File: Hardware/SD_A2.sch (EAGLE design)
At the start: 23 parts, among them IC1 74LS245N, IC2 LM1117DTX-3.3, IC3 28C64ASO, IC4 XC9572XL

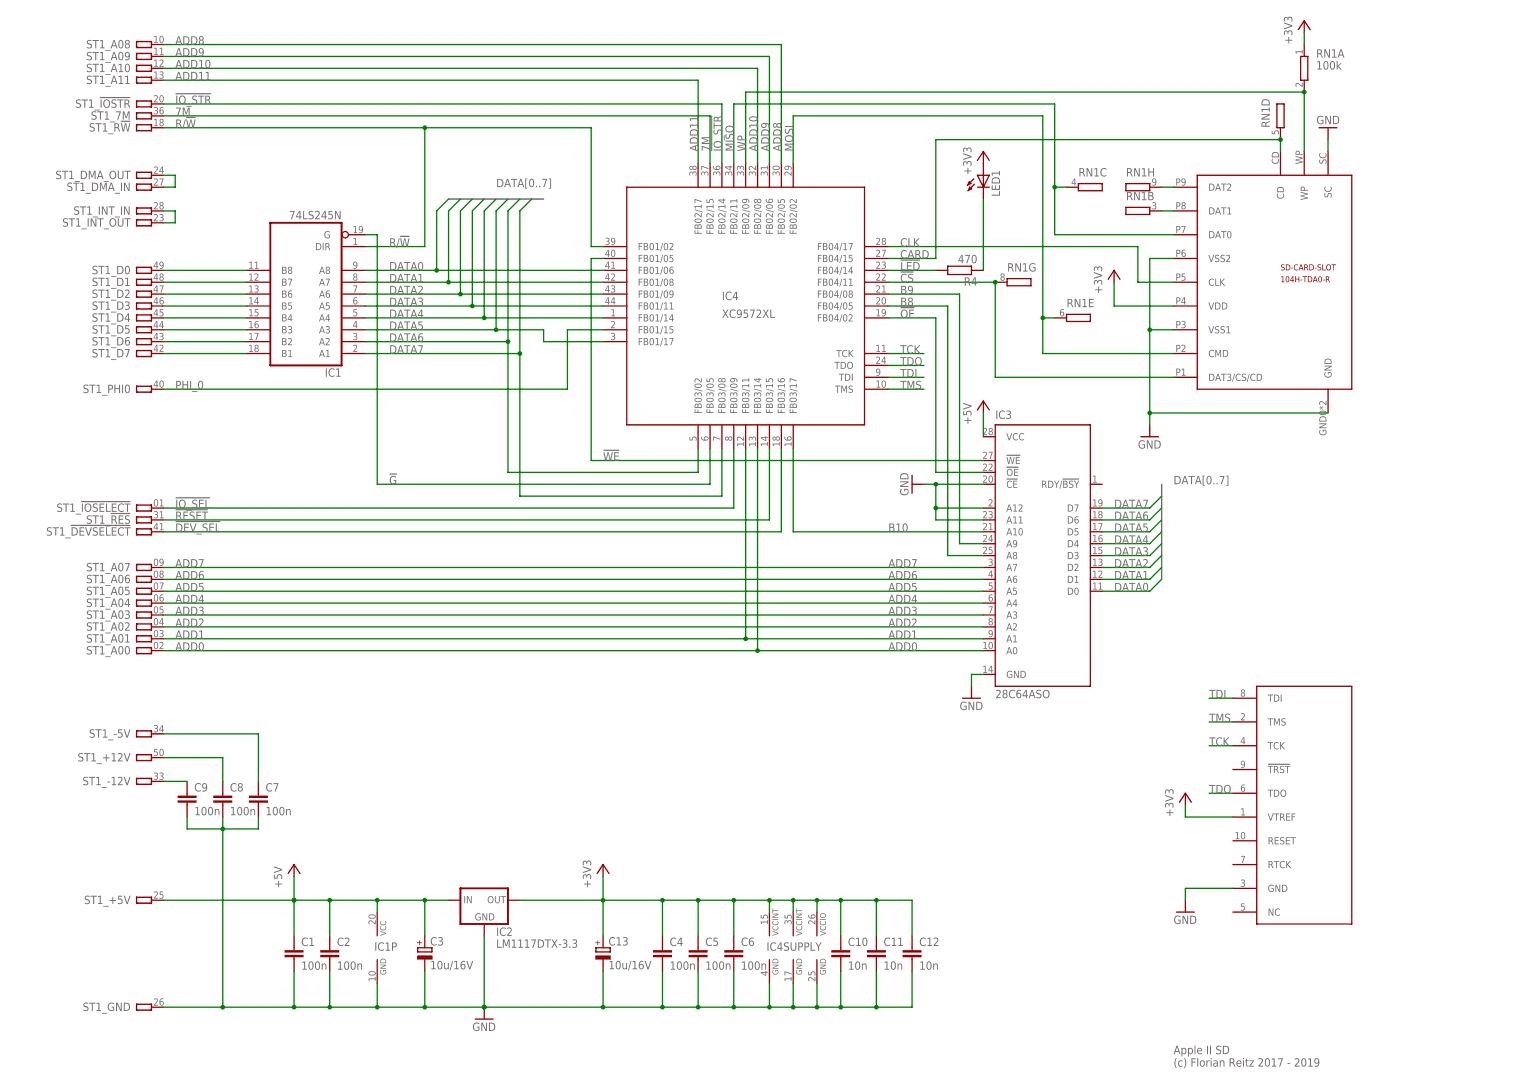
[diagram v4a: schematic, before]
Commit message: Pullup on /WE added
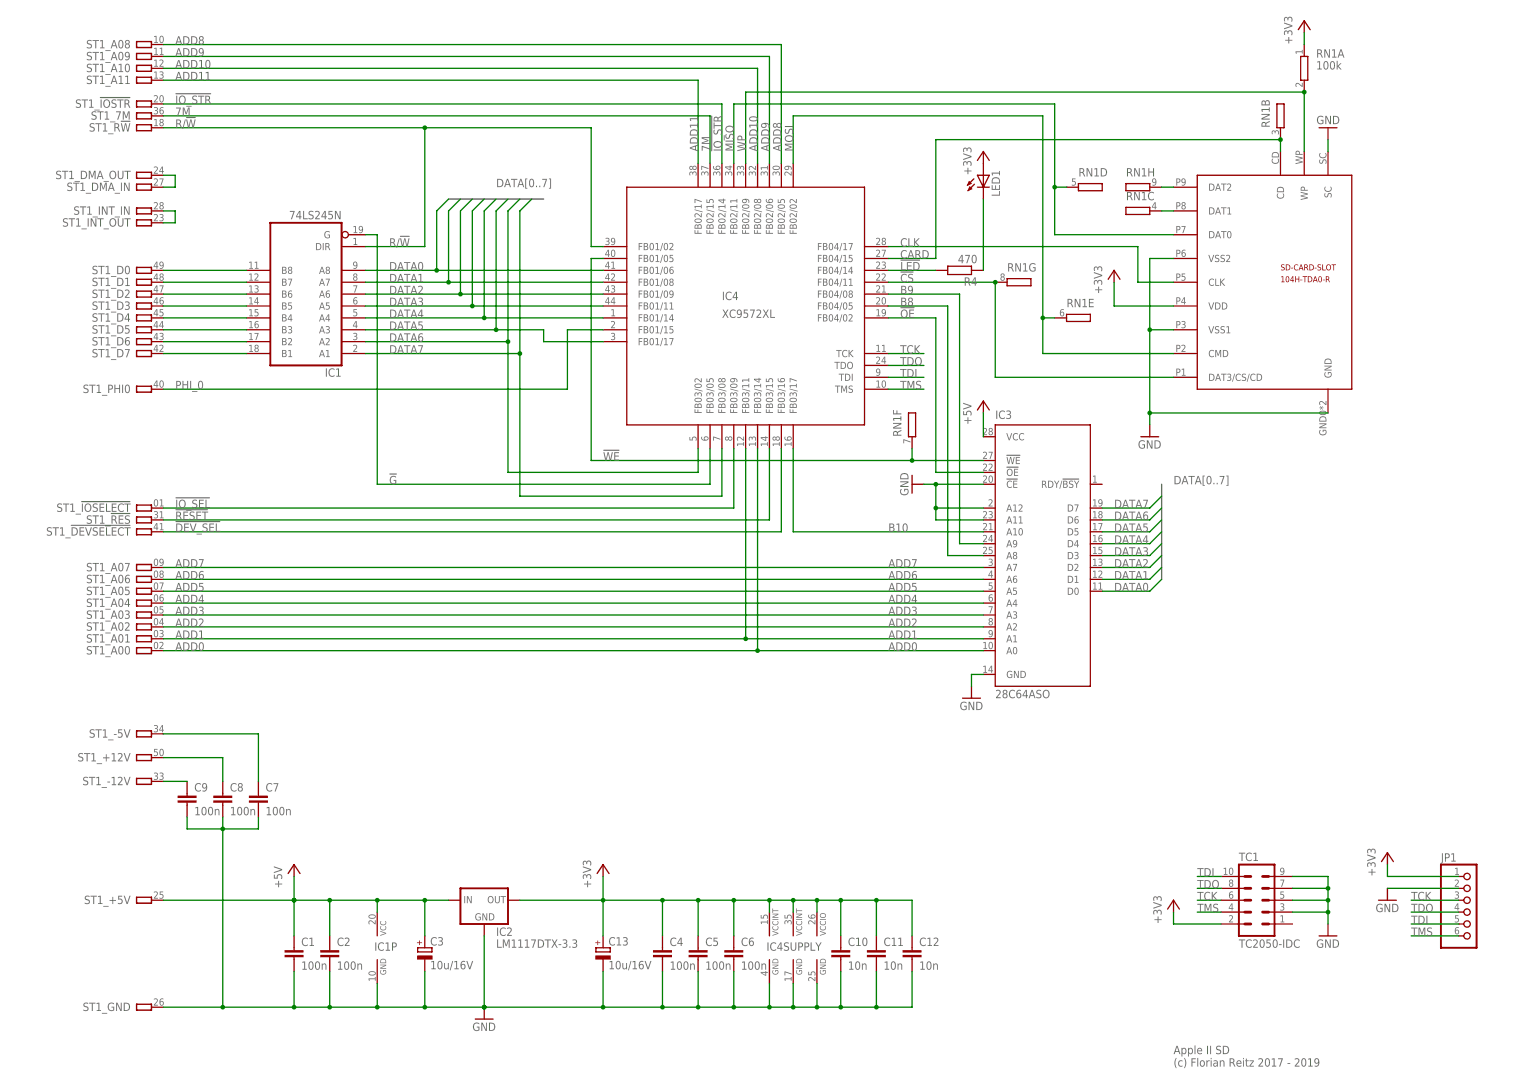
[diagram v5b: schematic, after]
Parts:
- removed U$1: TC2050-NL, eagle_tag-connect-2050:TC2050-NL
- added JP1: (no value), pinhead:PINHD-1X6
- added TC1: TC2050-IDC, TagConnect:TC2050-IDC
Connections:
- removed net DAT1: RN1B.2, U$2.DAT1
- new net N$2: RN1C.2, U$2.DAT1
- net !WE: now also RN1F.2
- net +3V3: now also JP1.1, TC1.2; no longer U$1.VTREF
- net CARD: now also RN1B.2; no longer RN1D.2
- net GND: now also JP1.2, TC1.3, TC1.5, TC1.7, TC1.9; no longer U$1.GND
- net MISO: now also RN1D.2; no longer RN1C.2
- net TCK: now also JP1.3, TC1.6; no longer U$1.TCK
- net TDI: now also JP1.5, TC1.10; no longer U$1.TDI
- net TDO: now also JP1.4, TC1.8; no longer U$1.TDO
- net TMS: now also JP1.6, TC1.4; no longer U$1.TMS
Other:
- moved on the sheet: RN1B, RN1C, RN1D
